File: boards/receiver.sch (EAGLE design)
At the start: 81 parts, among them IC2 7805DT, Q1 BC846BSMD, Q2 BC846BSMD, Q3 BC846BSMD, Q4 BC846BSMD, Q5 BC846BSMD, Q6 BC846BSMD, Q7 BC846BSMD, Q8 BC846BSMD

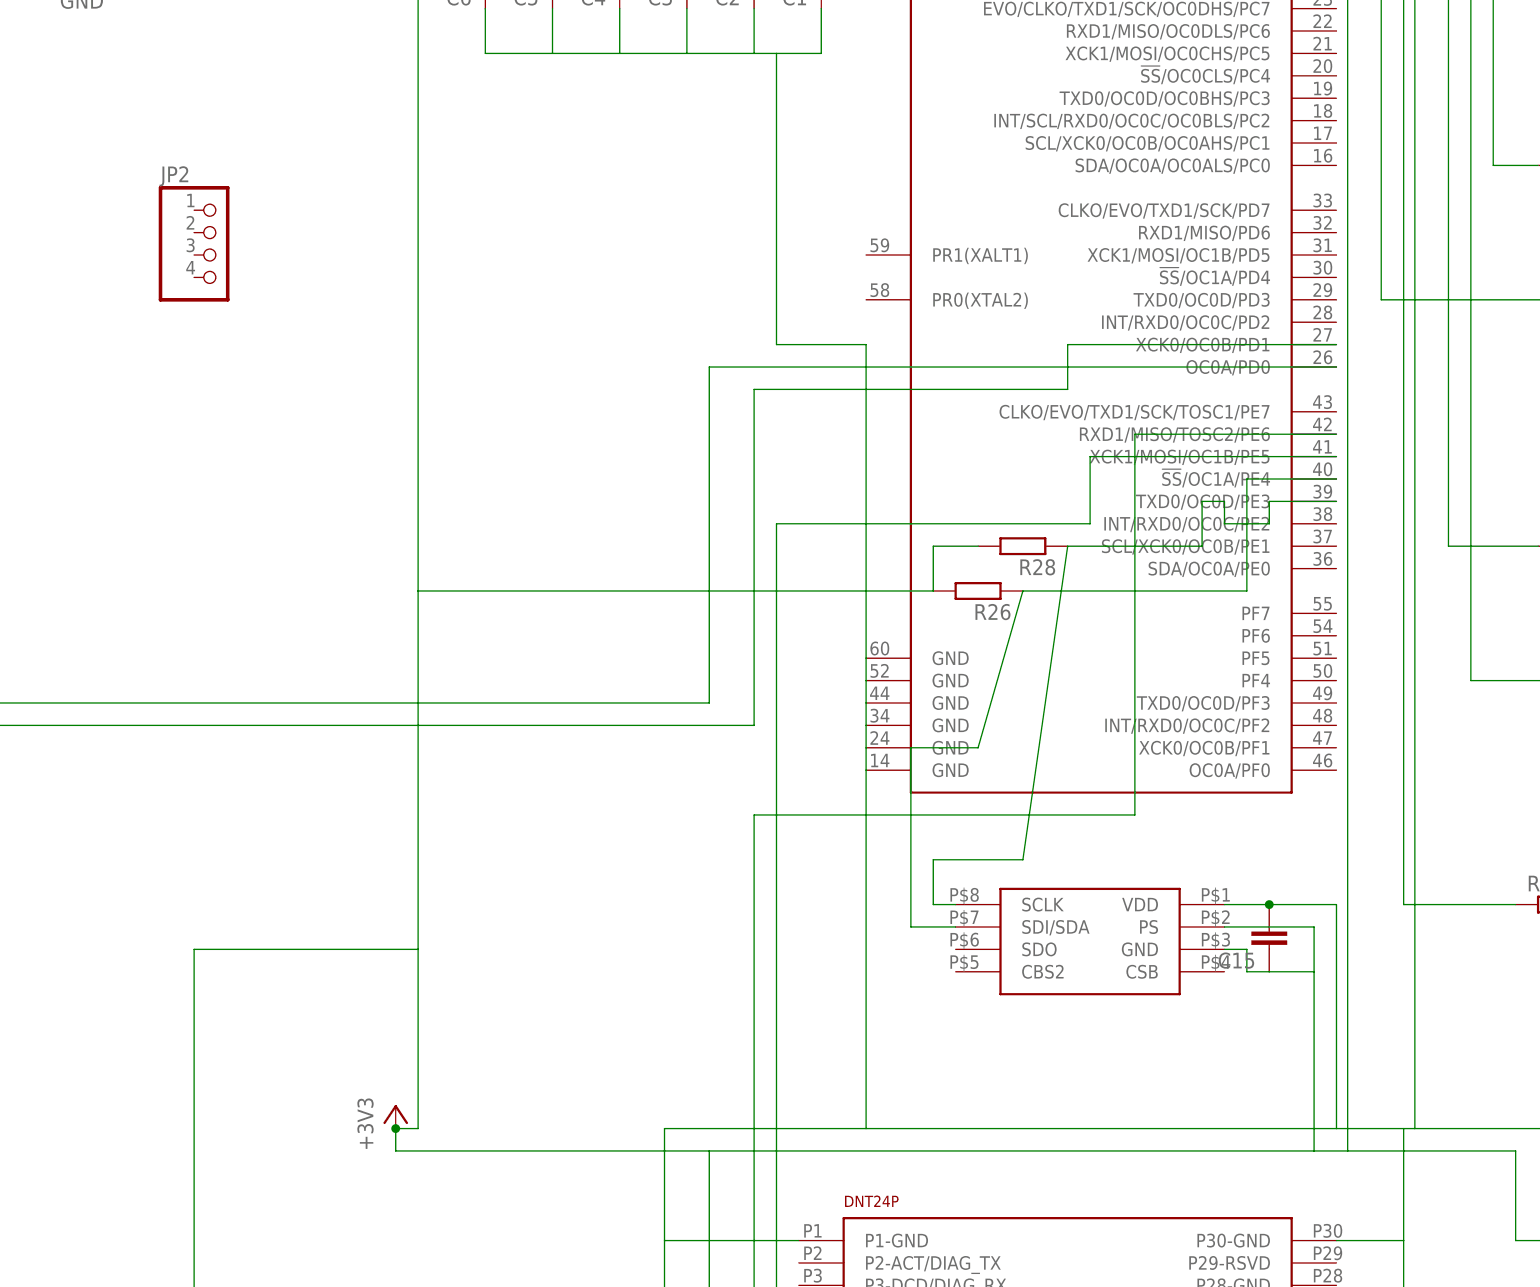
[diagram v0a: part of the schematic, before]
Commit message: Layout changes, all connections are routed now
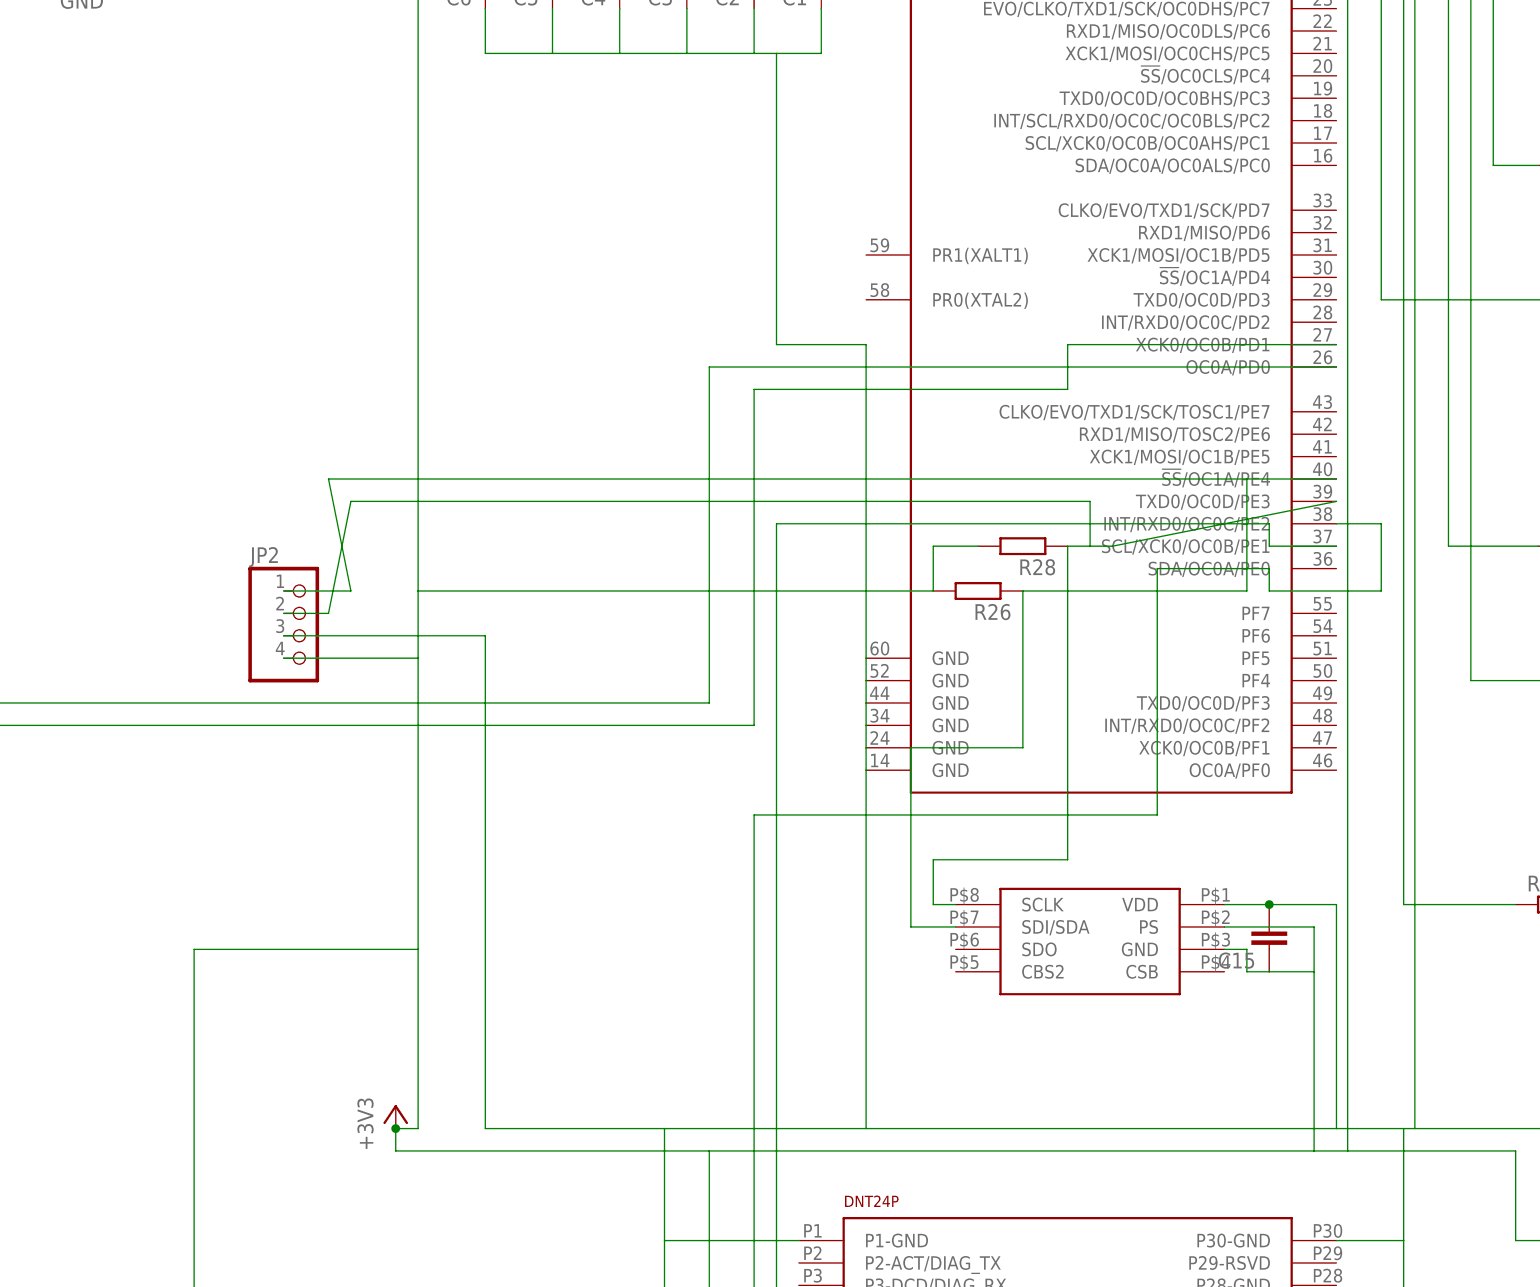
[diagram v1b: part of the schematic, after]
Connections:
- net +3V3: now also JP2.4
- net GND: now also JP2.3
- net N$33: now also IC3.SCL/XCK0/OC0B/PE1; no longer IC3.XCK1/MOSI/OC1B/PE5
- net N$36: now also IC3.INT/RXD0/OC0C/PE2; no longer IC3.RXD1/MISO/TOSC2/PE6
- net N$46: now also JP2.2
- net N$47: now also JP2.1
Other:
- moved on the sheet: JP2
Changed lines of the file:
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@@
 <instance part="TP4" gate="G$1" x="265.43" y="208.28" rot="R270"/>
 <instance part="JP1" gate="A" x="93.98" y="241.3" rot="R90"/>
-<instance part="JP2" gate="A" x="134.62" y="167.64"/>
+<instance part="JP2" gate="A" x="144.78" y="124.46"/>
 <instance part="GND6" gate="1" x="119.38" y="198.12"/>
 <instance part="R27" gate="G$1" x="88.9" y="215.9" rot="R90"/>
@@
 <wire x1="200.66" y1="45.72" x2="198.12" y2="45.72" width="0.1524" layer="91"/>
 <wire x1="198.12" y1="45.72" x2="198.12" y2="137.16" width="0.1524" layer="91"/>
-<wire x1="198.12" y1="137.16" x2="233.68" y2="137.16" width="0.1524" layer="91"/>
-<wire x1="233.68" y1="137.16" x2="233.68" y2="144.78" width="0.1524" layer="91"/>
-<pinref part="IC3" gate="G$1" pin="XCK1/MOSI/OC1B/PE5"/>
-<wire x1="233.68" y1="144.78" x2="261.62" y2="144.78" width="0.1524" layer="91"/>
+<wire x1="198.12" y1="137.16" x2="254" y2="137.16" width="0.1524" layer="91"/>
+<wire x1="254" y1="137.16" x2="254" y2="134.62" width="0.1524" layer="91"/>
+<pinref part="IC3" gate="G$1" pin="SCL/XCK0/OC0B/PE1"/>
+<wire x1="254" y1="134.62" x2="261.62" y2="134.62" width="0.1524" layer="91"/>
 </segment>
 </net>
@@
 <wire x1="200.66" y1="43.18" x2="195.58" y2="43.18" width="0.1524" layer="91"/>
 <wire x1="195.58" y1="43.18" x2="195.58" y2="104.14" width="0.1524" layer="91"/>
-<wire x1="195.58" y1="104.14" x2="238.76" y2="104.14" width="0.1524" layer="91"/>
-<wire x1="238.76" y1="104.14" x2="238.76" y2="147.32" width="0.1524" layer="91"/>
-<pinref part="IC3" gate="G$1" pin="RXD1/MISO/TOSC2/PE6"/>
-<wire x1="238.76" y1="147.32" x2="261.62" y2="147.32" width="0.1524" layer="91"/>
+<wire x1="195.58" y1="104.14" x2="241.3" y2="104.14" width="0.1524" layer="91"/>
+<wire x1="241.3" y1="104.14" x2="241.3" y2="132.08" width="0.1524" layer="91"/>
+<wire x1="241.3" y1="132.08" x2="254" y2="132.08" width="0.1524" layer="91"/>
+<wire x1="254" y1="132.08" x2="254" y2="129.54" width="0.1524" layer="91"/>
+<wire x1="254" y1="129.54" x2="266.7" y2="129.54" width="0.1524" layer="91"/>
+<wire x1="266.7" y1="129.54" x2="266.7" y2="137.16" width="0.1524" layer="91"/>
+<pinref part="IC3" gate="G$1" pin="INT/RXD0/OC0C/PE2"/>
+<wire x1="266.7" y1="137.16" x2="261.62" y2="137.16" width="0.1524" layer="91"/>
 </segment>
 </net>
@@
 <wire x1="154.94" y1="68.58" x2="157.48" y2="68.58" width="0.1524" layer="91"/>
 <wire x1="157.48" y1="68.58" x2="157.48" y2="88.9" width="0.1524" layer="91"/>
-<wire x1="157.48" y1="88.9" x2="157.48" y2="129.54" width="0.1524" layer="91"/>
+<wire x1="157.48" y1="88.9" x2="157.48" y2="121.92" width="0.1524" layer="91"/>
+<wire x1="157.48" y1="121.92" x2="157.48" y2="129.54" width="0.1524" layer="91"/>
 <wire x1="157.48" y1="129.54" x2="157.48" y2="213.36" width="0.1524" layer="91"/>
 <wire x1="193.04" y1="25.4" x2="190.5" y2="25.4" width="0.1524" layer="91"/>
@@
 <wire x1="215.9" y1="134.62" x2="215.9" y2="129.54" width="0.1524" layer="91"/>
 <wire x1="157.48" y1="129.54" x2="215.9" y2="129.54" width="0.1524" layer="91"/>
+<pinref part="JP2" gate="A" pin="4"/>
+<wire x1="157.48" y1="121.92" x2="142.24" y2="121.92" width="0.1524" layer="91"/>
 </segment>
 </net>
@@
 <pinref part="C15" gate="G$1" pin="2"/>
 <junction x="254" y="93.98"/>
+<wire x1="185.42" y1="68.58" x2="165.1" y2="68.58" width="0.1524" layer="91"/>
+<wire x1="165.1" y1="68.58" x2="165.1" y2="124.46" width="0.1524" layer="91"/>
+<wire x1="165.1" y1="124.46" x2="142.24" y2="124.46" width="0.1524" layer="91"/>
+<pinref part="JP2" gate="A" pin="3"/>
 </segment>
 <segment>
@@
 </segment>
 </net>
-<net name="N$46" class="0">
-<segment>
-<wire x1="231.14" y1="134.62" x2="226.06" y2="99.06" width="0.1524" layer="91"/>
-<wire x1="226.06" y1="99.06" x2="215.9" y2="99.06" width="0.1524" layer="91"/>
-<wire x1="215.9" y1="99.06" x2="215.9" y2="93.98" width="0.1524" layer="91"/>
-<pinref part="U$2" gate="G$1" pin="SCLK"/>
-<wire x1="215.9" y1="93.98" x2="218.44" y2="93.98" width="0.1524" layer="91"/>
-<pinref part="R28" gate="G$1" pin="1"/>
-<wire x1="231.14" y1="134.62" x2="246.38" y2="134.62" width="0.1524" layer="91"/>
-<wire x1="246.38" y1="134.62" x2="246.38" y2="139.7" width="0.1524" layer="91"/>
-<wire x1="246.38" y1="139.7" x2="248.92" y2="139.7" width="0.1524" layer="91"/>
-<wire x1="248.92" y1="139.7" x2="248.92" y2="137.16" width="0.1524" layer="91"/>
-<wire x1="248.92" y1="137.16" x2="254" y2="137.16" width="0.1524" layer="91"/>
-<wire x1="254" y1="137.16" x2="254" y2="139.7" width="0.1524" layer="91"/>
-<pinref part="IC3" gate="G$1" pin="TXD0/OC0D/PE3"/>
-<wire x1="254" y1="139.7" x2="261.62" y2="139.7" width="0.1524" layer="91"/>
-</segment>
-</net>
 <net name="N$47" class="0">
 <segment>
@@
 <wire x1="218.44" y1="91.44" x2="213.36" y2="91.44" width="0.1524" layer="91"/>
 <wire x1="213.36" y1="91.44" x2="213.36" y2="111.76" width="0.1524" layer="91"/>
-<wire x1="213.36" y1="111.76" x2="220.98" y2="111.76" width="0.1524" layer="91"/>
-<wire x1="220.98" y1="111.76" x2="226.06" y2="129.54" width="0.1524" layer="91"/>
+<wire x1="213.36" y1="111.76" x2="226.06" y2="111.76" width="0.1524" layer="91"/>
+<wire x1="226.06" y1="111.76" x2="226.06" y2="129.54" width="0.1524" layer="91"/>
 <pinref part="R26" gate="G$1" pin="1"/>
 <wire x1="226.06" y1="129.54" x2="251.46" y2="129.54" width="0.1524" layer="91"/>
@@
 <pinref part="IC3" gate="G$1" pin="!SS!/OC1A/PE4"/>
 <wire x1="251.46" y1="142.24" x2="261.62" y2="142.24" width="0.1524" layer="91"/>
-</segment>
-</net>
+<wire x1="251.46" y1="142.24" x2="147.32" y2="142.24" width="0.1524" layer="91"/>
+<pinref part="JP2" gate="A" pin="1"/>
+<wire x1="149.86" y1="129.54" x2="142.24" y2="129.54" width="0.1524" layer="91"/>
+<wire x1="147.32" y1="142.24" x2="149.86" y2="129.54" width="0.1524" layer="91"/>
+</segment>
+</net>
+<net name="N$46" class="0">
+<segment>
+<pinref part="JP2" gate="A" pin="2"/>
+<wire x1="147.32" y1="127" x2="142.24" y2="127" width="0.1524" layer="91"/>
+<wire x1="233.68" y1="139.7" x2="149.86" y2="139.7" width="0.1524" layer="91"/>
+<wire x1="231.14" y1="134.62" x2="231.14" y2="99.06" width="0.1524" layer="91"/>
+<wire x1="231.14" y1="99.06" x2="215.9" y2="99.06" width="0.1524" layer="91"/>
+<wire x1="215.9" y1="99.06" x2="215.9" y2="93.98" width="0.1524" layer="91"/>
+<pinref part="U$2" gate="G$1" pin="SCLK"/>
+<wire x1="215.9" y1="93.98" x2="218.44" y2="93.98" width="0.1524" layer="91"/>
+<pinref part="R28" gate="G$1" pin="1"/>
+<wire x1="231.14" y1="134.62" x2="233.68" y2="134.62" width="0.1524" layer="91"/>
+<pinref part="IC3" gate="G$1" pin="TXD0/OC0D/PE3"/>
+<wire x1="233.68" y1="134.62" x2="236.22" y2="134.62" width="0.1524" layer="91"/>
+<wire x1="236.22" y1="134.62" x2="261.62" y2="139.7" width="0.1524" layer="91"/>
+<wire x1="233.68" y1="139.7" x2="233.68" y2="134.62" width="0.1524" layer="91"/>
+<wire x1="147.32" y1="127" x2="149.86" y2="139.7" width="0.1524" layer="91"/>
+</segment>
+</net>

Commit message: Added some passives for the voltage regulator.
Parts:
- removed IC2: 7805DT, linear:7805DT
- added C17, C19: 10µF, eagle-ltspice:CC0603
- added C18, C21: 100nF, eagle-ltspice:CC0603
- added D8: B 140 F, diode:CGRM4001-G
- added IC1: 7805DT, linear:7805DT
- C1, C11, C15, C16, C2, C3, C4, C5, C6, C7, C8, C9: value (none) -> 100nF
- C10: value (none) -> 2.2nF
- C12, C13: value (none) -> 0.1µF
- C14: value (none) -> 10nF
- IC3: value (none) -> XMEGA128a3u
- JP1: value (none) -> vSense
- JP2: value (none) -> i2c
- R1, R10, R11, R12, R13, R14, R15, R16, R17, R2, R20, R22, R23, R24, R25, R26, R28, R3, R4, R5, R6, R7, R8, R9: value (none) -> 10k
- R18, R19, R21, R27: value (none) -> 560
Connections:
- removed net +3V3: C1.2, C12.2, C14.2, C15.1, C2.2, C3.2, C4.2, C5.2, C6.2, C9.2, IC2.VO, IC3.AVCC, IC3.VCC@1, IC3.VCC@2, IC3.VCC@3, IC3.VCC@4, IC3.VCC@5, JP2.4, R17.1, R20.1, R26.2, R28.2, TP4.TP, U$1.P14-VCC, U$2.GND, U$2.PS, U$3.P13-VDD, U$3.P8-VLOGIC
- removed net N$34: D1.C, D11.C, D2.C, D3.C, D4.C, D5.C, D6.C, D7.C, IC2.VI
- new net VCC: C1.2, C12.2, C14.2, C15.1, C18.2, C19.2, C2.2, C3.2, C4.2, C5.2, C6.2, C9.2, D8.A, IC1.VO, IC3.AVCC, IC3.VCC@1, IC3.VCC@2, IC3.VCC@3, IC3.VCC@4, IC3.VCC@5, JP2.4, R17.1, R20.1, R26.2, R28.2, TP4.TP, U$1.P14-VCC, U$2.GND, U$2.PS, U$3.P13-VDD, U$3.P8-VLOGIC
- new net VDD: C17.2, C21.2, D1.C, D11.C, D2.C, D3.C, D4.C, D5.C, D6.C, D7.C, D8.C, IC1.VI
- net GND: now also C17.1, C18.1, C19.1, C21.1, IC1.GND; no longer IC2.GND
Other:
- moved on the sheet: R13
